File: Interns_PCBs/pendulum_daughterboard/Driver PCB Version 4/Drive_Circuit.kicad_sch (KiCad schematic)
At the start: 12 parts, among them IC5 MAX9928FAUA+, J2 Coil, Q1 BC858W, Q2 BD911

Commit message: Another Drive PCB
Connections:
- net D_5V is gone; now on net PEND_3.3V: C9.1, NT2.2
- net D_GND is gone; now on net GND: C9.2, IC5.7 (GND)
- net DRIVE_5V renamed PEND_3.3V
- net DRIVE_GND renamed GND
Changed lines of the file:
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@@
     (stroke (width 0) (type default) (color 0 0 0 0))
   )
-  (hierarchical_label "D_GND" (shape input) (at 269.24 77.47 0)
+  (hierarchical_label "GND" (shape input) (at 269.24 77.47 0)
     (effects (font (size 1.27 1.27)) (justify left))
   )
@@
     (effects (font (size 1.27 1.27)) (justify right))
   )
-  (hierarchical_label "D_5V" (shape input) (at 279.4 66.04 90)
+  (hierarchical_label "PEND_3.3V" (shape input) (at 279.4 66.04 90)
     (effects (font (size 1.27 1.27)) (justify left))
   )
-  (hierarchical_label "D_GND" (shape input) (at 279.4 97.79 270)
+  (hierarchical_label "GND" (shape input) (at 279.4 97.79 270)
     (effects (font (size 1.27 1.27)) (justify right))
   )
@@
     (effects (font (size 1.27 1.27)) (justify right))
   )
-  (hierarchical_label "DRIVE_5V" (shape input) (at 66.04 74.93 90)
+  (hierarchical_label "PEND_3.3V" (shape input) (at 66.04 74.93 90)
     (effects (font (size 1.27 1.27)) (justify left))
   )
-  (hierarchical_label "DRIVE_GND" (shape input) (at 133.35 115.57 270)
+  (hierarchical_label "GND" (shape input) (at 133.35 115.57 270)
     (effects (font (size 1.27 1.27)) (justify right))
   )

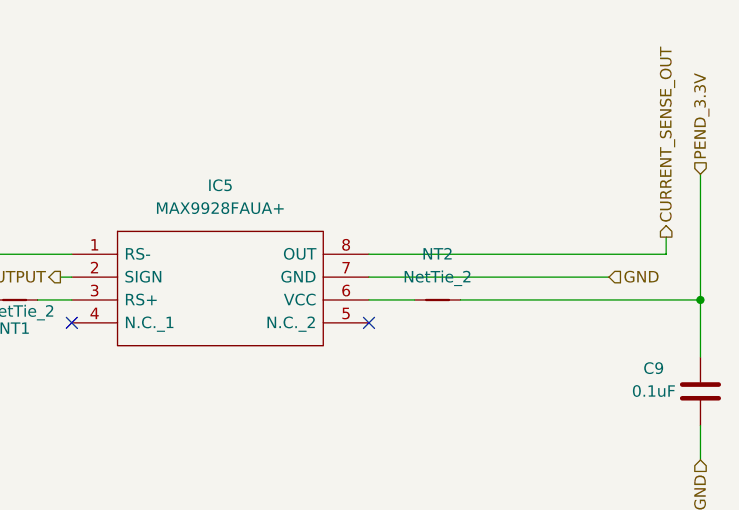
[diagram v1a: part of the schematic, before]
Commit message: 3.3V PCB Design
PCB with 2 voltage regulators, regulating both the 5V input from the digital pins and the external 5V from the terminal block.
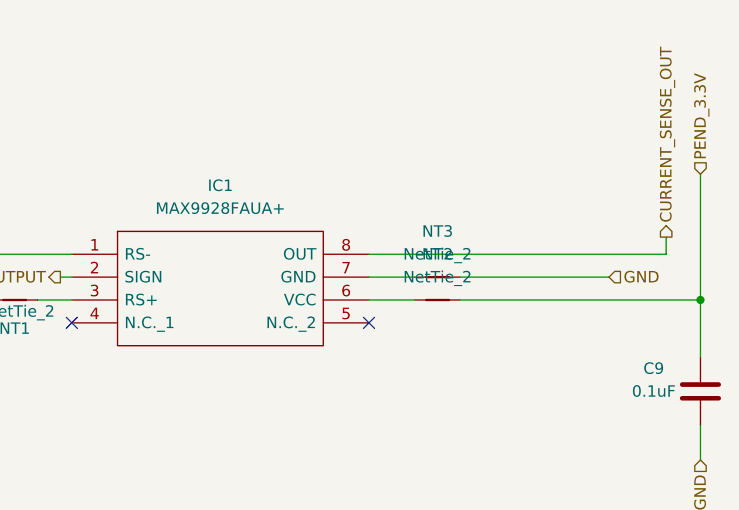
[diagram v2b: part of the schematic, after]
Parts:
- added NT3: NetTie_2, NetTie:NetTie-2_SMD_Pad0.5mm, symbol Device:NetTie_2
- renumbered IC5 to IC1
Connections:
- net GND: now also NT3.2; no longer IC1.7 (GND)
- new net: IC1.7 (GND), NT3.1
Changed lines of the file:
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@@
     (stroke (width 0) (type default) (color 0 0 0 0))
   )
-  (wire (pts (xy 242.57 77.47) (xy 269.24 77.47))
+  (wire (pts (xy 242.57 77.47) (xy 247.65 77.47))
     (stroke (width 0) (type default) (color 0 0 0 0))
   )
@@
   )
   (wire (pts (xy 113.03 74.93) (xy 113.03 86.36))
+    (stroke (width 0) (type default) (color 0 0 0 0))
+  )
+  (wire (pts (xy 252.73 77.47) (xy 269.24 77.47))
     (stroke (width 0) (type default) (color 0 0 0 0))
   )
@@
     (pin "2")
   )
+  (symbol (lib_id "Device:NetTie_2") (at 250.19 77.47 0) (unit 1)
+    (in_bom yes) (on_board yes) (fields_autoplaced)
+    (property "Reference" "NT3" (id 0) (at 250.19 72.39 0))
+    (property "Value" "NetTie_2" (id 1) (at 250.19 74.93 0))
+    (property "Footprint" "NetTie:NetTie-2_SMD_Pad0.5mm" (id 2) (at 250.19 77.47 0)
+      (effects (font (size 1.27 1.27)) hide)
+    )
+    (property "Datasheet" "~" (id 3) (at 250.19 77.47 0)
+      (effects (font (size 1.27 1.27)) hide)
+    )
+    (pin "1")
+    (pin "2")
+  )
   (symbol (lib_id "Device:NetTie_2") (at 250.19 80.01 0) (unit 1)
     (in_bom yes) (on_board yes) (fields_autoplaced)
@@
   (symbol (lib_id "MAX9928FAUA+:MAX9928FAUA+") (at 209.55 74.93 0) (unit 1)
     (in_bom yes) (on_board yes) (fields_autoplaced)
-    (property "Reference" "IC5" (id 0) (at 226.06 67.31 0))
+    (property "Reference" "IC1" (id 0) (at 226.06 67.31 0))
     (property "Value" "MAX9928FAUA+" (id 1) (at 226.06 69.85 0))
     (property "Footprint" "Sensor_Current:SOP65P490X110-8N" (id 2) (at 238.76 72.39 0)
